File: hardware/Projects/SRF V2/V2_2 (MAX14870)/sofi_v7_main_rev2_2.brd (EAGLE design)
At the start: 59.7 x 65.7 mm, 82 parts

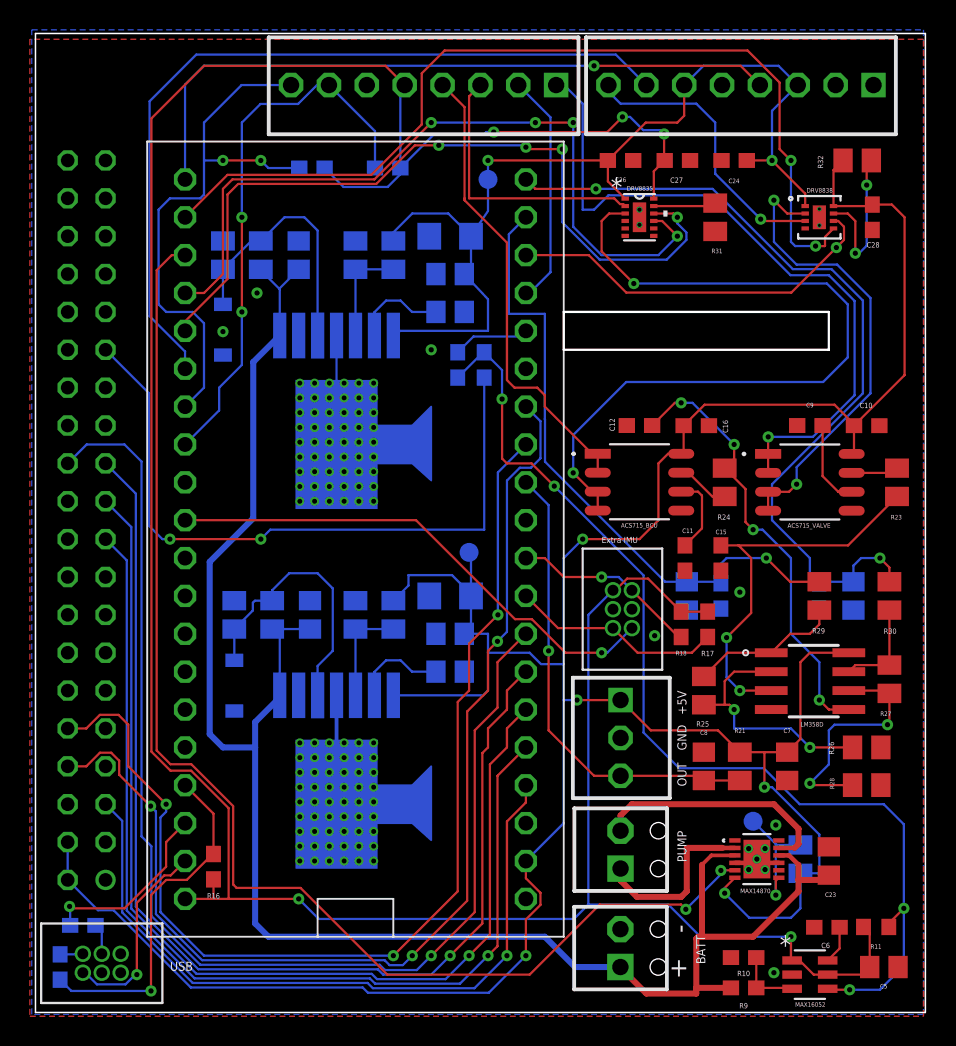
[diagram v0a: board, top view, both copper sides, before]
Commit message: added GND plane vias to minimize current return paths, modified 2POS_BLOCK lib
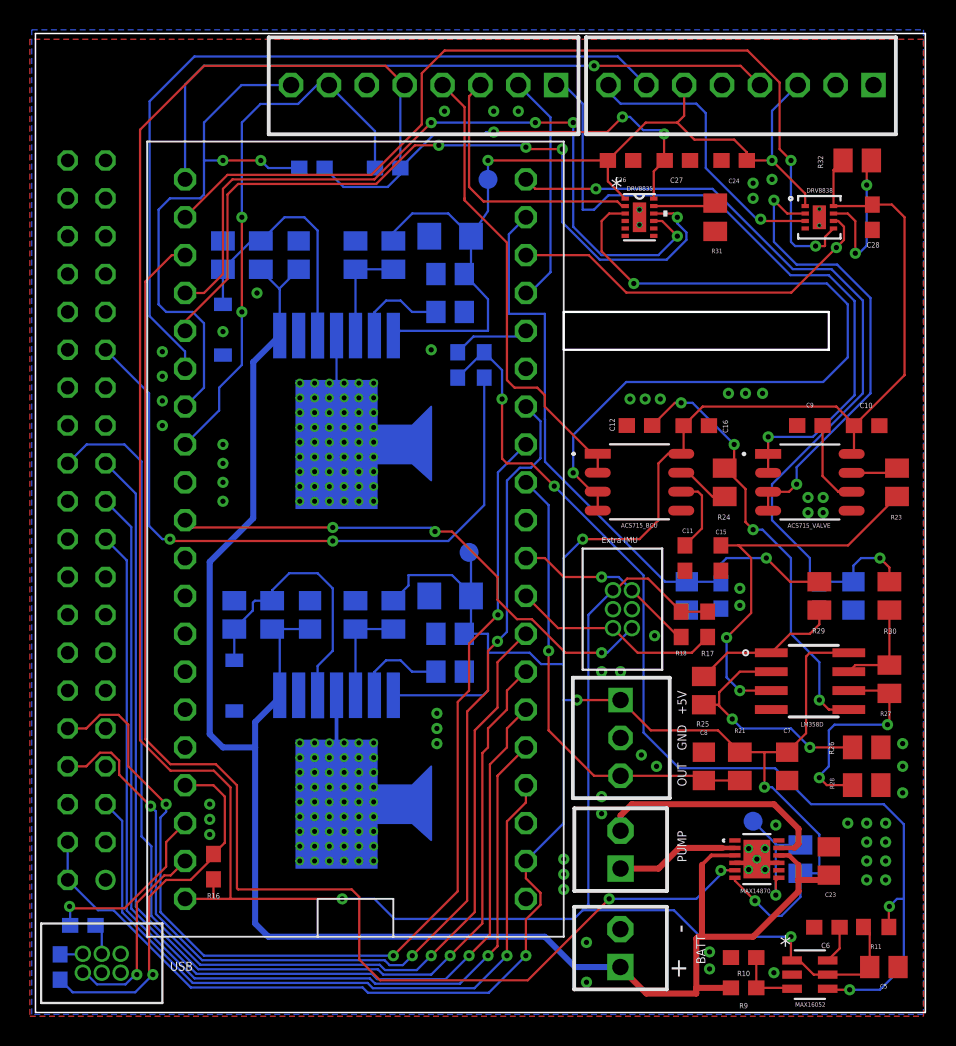
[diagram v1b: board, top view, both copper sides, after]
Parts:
- BATT, PUMP: value 2POS_BLOCK -> 2POS_BLOCK2POS_BLOCK_NOSTANDS; device 2pos_block_terminal:2POS_BLOCK -> 2pos_block_terminal:2POS_BLOCK_NOSTANDS
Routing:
- net PUMP_MOTOR_PWM: track 85.9 -> 90.0 mm
- net PUMP_MOTOR_V1: track 12.0 -> 8.24 mm
- net 6V: track 65.6 -> 63.0 mm
- net 5V: track 196.6 -> 194.5 mm
- net 3.3V: track 194.0 -> 195.8 mm
- net D+: track 23.6 -> 25.2 mm
- net N$27: track 16.0 -> 14.9 mm
- net LVD_OUT: track 70.4 -> 71.3 mm
- net INT_MOV: track 34.3 -> 35.2 mm, vias 1 -> 3
- net N$1: track 46.3 -> 45.5 mm
- net N$25: track 16.9 -> 16.1 mm
- net GND: vias 7 -> 63

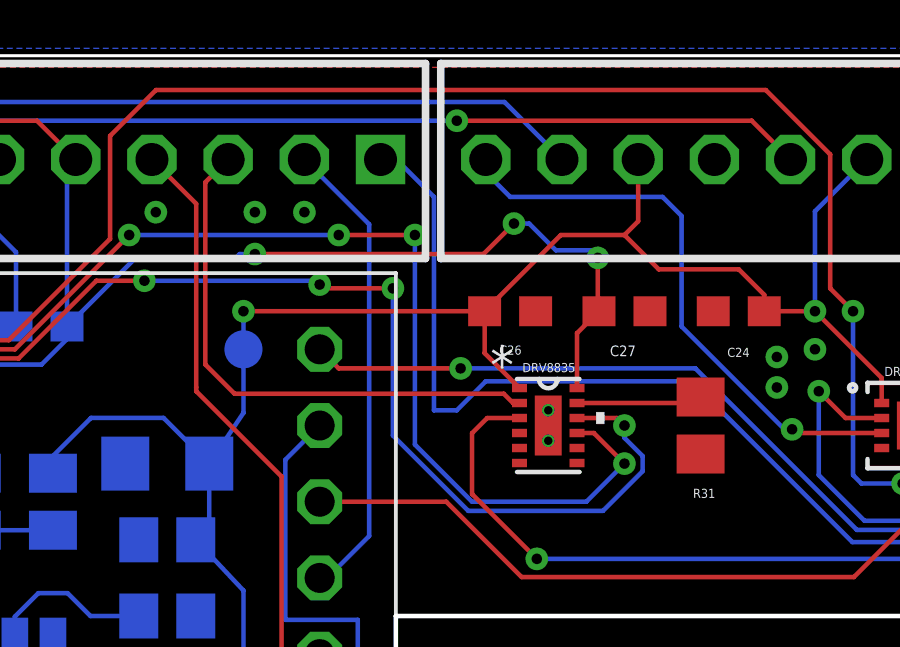
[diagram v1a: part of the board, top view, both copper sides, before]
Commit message: new motor driver footprints with extended pads, thermals test
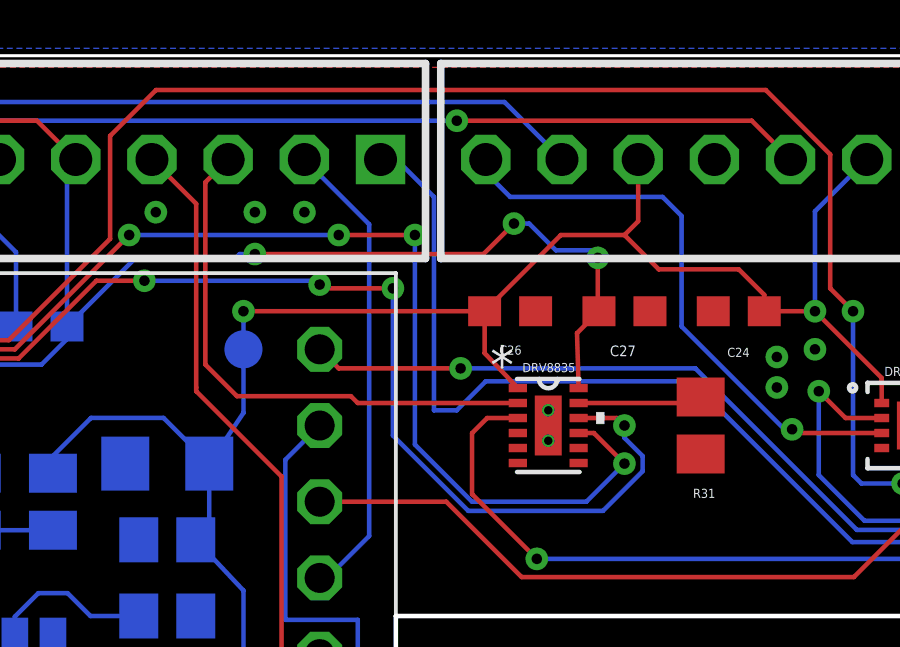
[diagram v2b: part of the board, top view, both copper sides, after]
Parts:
- DRV8835: value DRV8835DSSRDSS12_P9X2_THERMAL -> DRV8835DSSRDSS12_P9X2_THERMAL_EXTENDED; device DRV8835_ultra_librarian:DSS12_P9X2_THERMAL -> DRV8835_ultra_librarian:DSS12_P9X2_THERMAL_EXTENDED

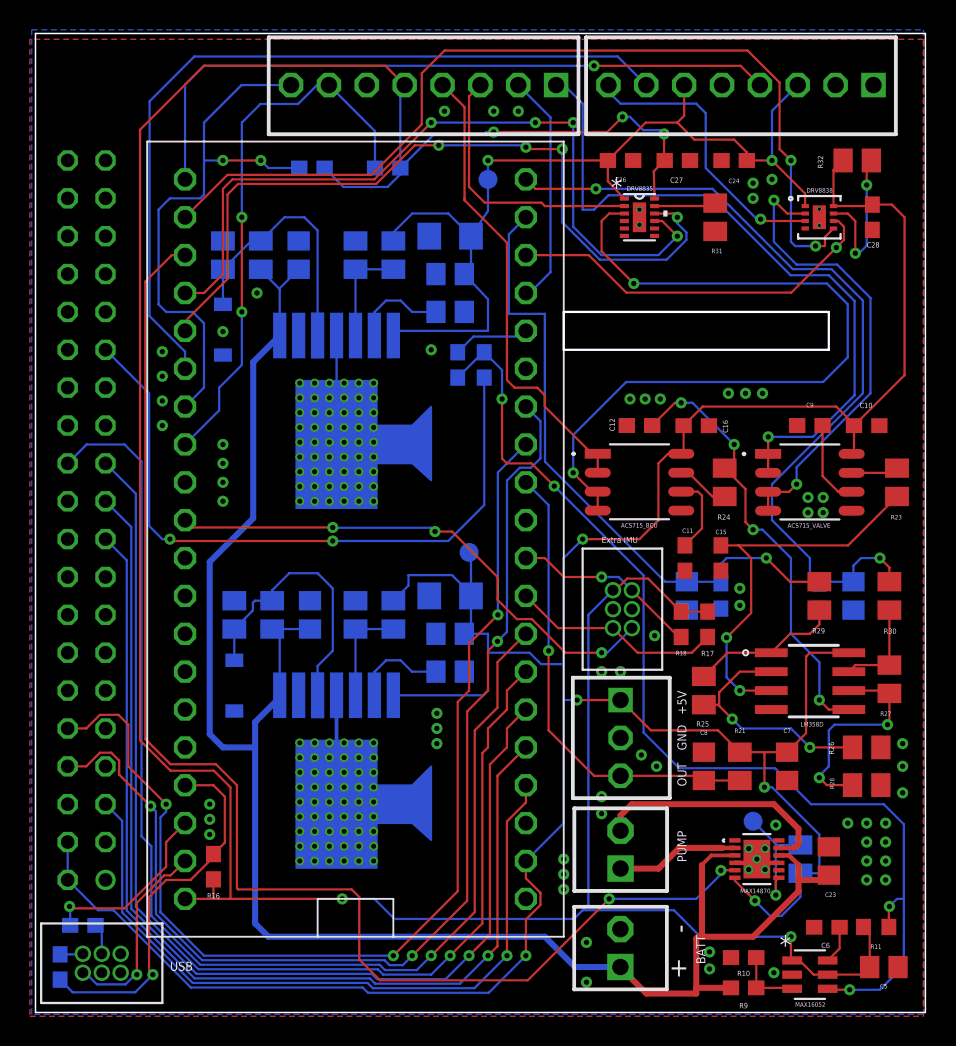
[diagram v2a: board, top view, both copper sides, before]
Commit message: added power planes for VCC to power modules, pump motor outputs
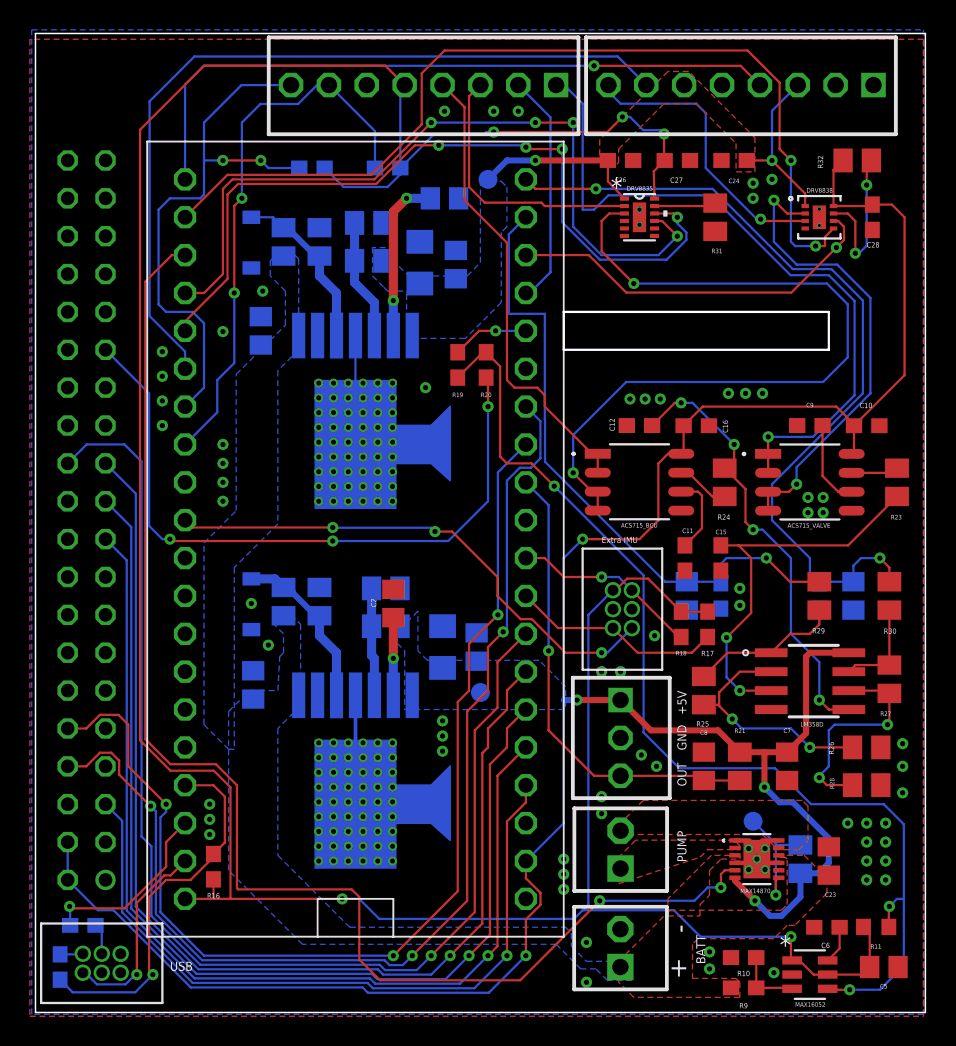
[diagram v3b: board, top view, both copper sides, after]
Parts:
- moved 5V 9.43 mm to (33.8, 24.0)
- moved C4 7.63 mm to (31.4, 57.1)
- moved R8 6.54 mm to (23.0, 54.2)
- moved D2 6.14 mm to (18.4, 55.9)
- moved C1 6.05 mm to (18.5, 24.5)
- moved C2 5.95 mm to (27.9, 30.0), flipped to the top, turned to 90 degrees
- moved R4 5.78 mm to (23.0, 30.1)
- moved C3 5.68 mm to (19.1, 48.3)
- moved D1 5.58 mm to (18.4, 31.6)
- moved C13 3.47 mm to (31.2, 27.1), turned to 90 degrees
- moved C14 2.70 mm to (29.7, 52.8), turned to 90 degrees
- moved R2 2.70 mm to (27.4, 31.0), turned to 180 degrees
- moved R6 2.33 mm to (26.3, 55.5), turned to 180 degrees
- moved C17 1.99 mm to (33.5, 27.1), turned to 90 degrees
- moved R7 1.76 mm to (20.6, 54.2)
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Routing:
- net VCC: track 120.7 -> 0.00 mm
- net 6V: track 62.9 -> 23.0 mm
- net 5V: track 194.5 -> 165.3 mm
- net PUMP_MOTOR_V2: track 16.4 -> 0.00 mm
- net PUMP_MOTOR_V1: track 8.24 -> 0.00 mm
- net N$8: track 19.0 -> 11.4 mm
- net N$13: track 17.6 -> 11.5 mm
- net N$9: track 6.33 -> 11.2 mm, vias 0 -> 2
- net GND: track 17.8 -> 21.5 mm, vias 63 -> 64
- net N$11: track 6.33 -> 5.21 mm, vias 0 -> 1
- net N$10: track 6.99 -> 8.11 mm
- net N$1: track 45.5 -> 45.6 mm, vias 2 -> 3
- net LVD_OUT: vias 4 -> 3
- net N$19: vias 0 -> 1
- added copper zone on layer 16, net 5V
- added copper zone on layer 1, net 6V
- added copper zone on layer 16, net 6V
- added copper zone on layer 1, net PUMP_MOTOR_V1
- added copper zone on layer 1, net PUMP_MOTOR_V2
- added copper zone on layer 1, net VCC
- added copper zone on layer 16, net VCC
